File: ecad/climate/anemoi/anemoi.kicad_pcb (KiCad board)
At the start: 2 copper layers, 45 x 30 mm, 21 parts, among them J1 215079-4, SW1 219-3MST, U1 TMP1075DGK, U2 MMA8453Q, U3 HIH6131-021-001

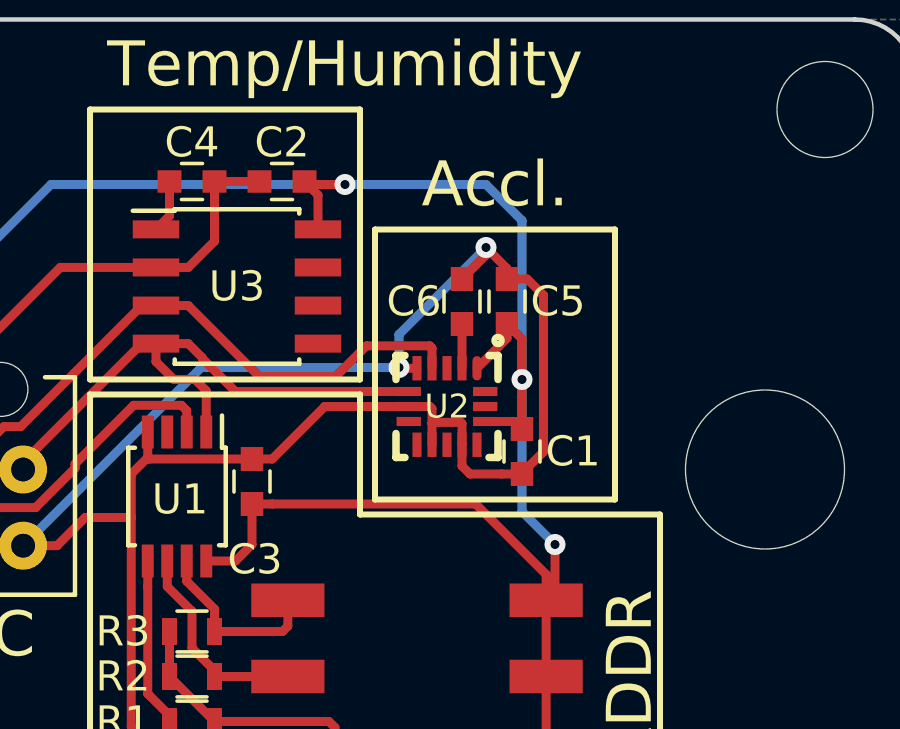
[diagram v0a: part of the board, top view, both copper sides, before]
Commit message: Updates Via size to conform to Factory Capabilities
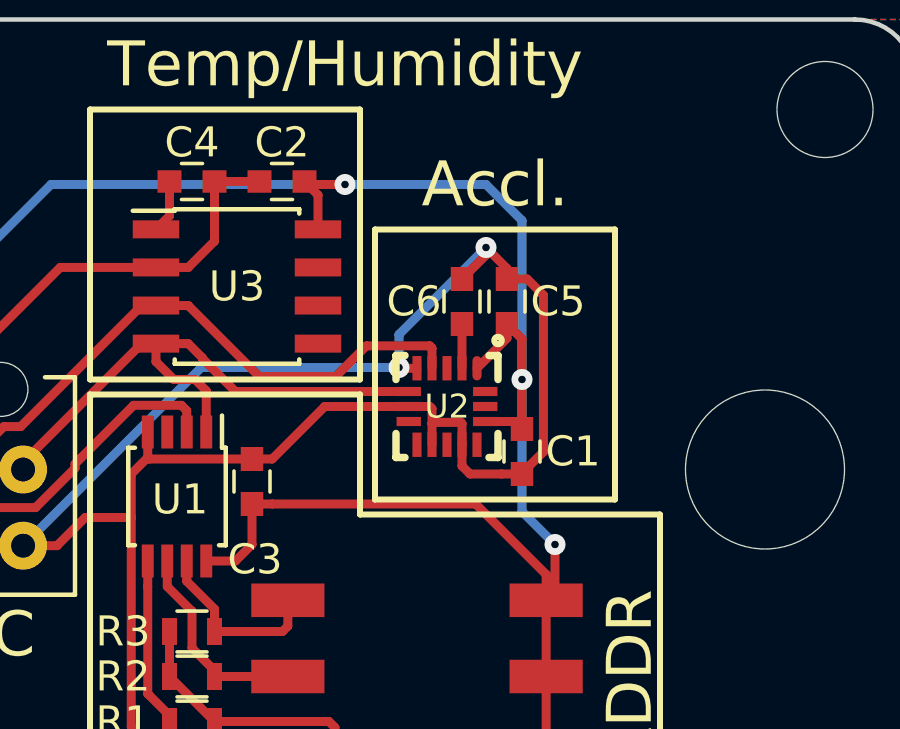
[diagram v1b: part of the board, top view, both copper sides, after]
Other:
- net class Default: via_drill 0.3 -> 0.25
- rule via_min_drill: 0.3 -> 0.25
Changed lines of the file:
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@@
-(kicad_pcb (version 4) (host pcbnew 4.0.7+dfsg1-1~bpo9+1)
+(kicad_pcb (version 20171130) (host pcbnew 5.0.0+dfsg1-2~bpo9+1)
   (general
-    (links 40)
-    (no_connects 0)
-    (area 69.924999 84.924999 115.075001 115.075001)
     (thickness 1.6)
     (drawings 30)
@@
     (edge_width 0.15)
     (via_size 0.7)
-    (via_drill 0.3)
+    (via_drill 0.25)
     (via_min_size 0.4)
-    (via_min_drill 0.3)
+    (via_min_drill 0.25)
     (uvia_size 0.3)
     (uvia_drill 0.1)
@@
       (layerselection 0x00030_80000001)
       (usegerberextensions false)
+      (usegerberattributes false)
+      (usegerberadvancedattributes false)
+      (creategerberjobfile false)
       (excludeedgelayer true)
       (linewidth 0.100000)
@@
       (hpglpennumber 1)
       (hpglpenspeed 20)
-      (hpglpendiameter 15)
-      (hpglpenoverlay 2)
+      (hpglpendiameter 15.000000)
       (psnegative false)
       (psa4output false)
@@
     (trace_width 0.3)
     (via_dia 0.7)
-    (via_drill 0.3)
+    (via_drill 0.25)
     (uvia_dia 0.3)
     (uvia_drill 0.1)
@@
     (tags "capacitor 0603")
     (attr smd)
-    (fp_text reference C1 (at 0 -1.7 360) (layer F.SilkS)
+    (fp_text reference C1 (at 0 -1.7) (layer F.SilkS)
       (effects (font (size 1 1) (thickness 0.15)))
     )
@@
     (tags "SSOP 0.65")
     (attr smd)
-    (fp_text reference U1 (at 0.1 -0.1 540) (layer F.SilkS)
+    (fp_text reference U1 (at 0.1 -0.1 180) (layer F.SilkS)
       (effects (font (size 1 1) (thickness 0.15)))
     )
@@
   (module FORT:Freescale_98ASA00063D_3x3mm_Pitch_0.5mm (layer F.Cu)
     (at 99.4 97.9 270)
-    (fp_text reference U2 (at 0 0 360) (layer F.SilkS)
+    (fp_text reference U2 (at 0 0) (layer F.SilkS)
       (effects (font (size 0.8 0.8) (thickness 0.15)))
     )
@@
   (segment (start 100.7 92.6) (end 100.7 92.85) (width 0.3) (layer F.Cu) (net 1))
   (segment (start 100.7 92.85) (end 99.9 93.65) (width 0.3) (layer F.Cu) (net 1))
-  (via (at 100.7 92.6) (size 0.7) (drill 0.3) (layers F.Cu B.Cu) (net 1))
+  (via (at 100.7 92.6) (size 0.7) (drill 0.25) (layers F.Cu B.Cu) (net 1))
   (segment (start 98.4 96.625) (end 97.825 96.625) (width 0.3) (layer F.Cu) (net 1))
-  (via (at 97.8 96.6) (size 0.7) (drill 0.3) (layers F.Cu B.Cu) (net 1))
+  (via (at 97.8 96.6) (size 0.7) (drill 0.25) (layers F.Cu B.Cu) (net 1))
   (segment (start 97.825 96.625) (end 97.8 96.6) (width 0.3) (layer F.Cu) (net 1))
   (segment (start 92.9 99.65) (end 89.475 99.65) (width 0.3) (layer F.Cu) (net 1))
@@
   (segment (start 101.9 97) (end 101.9 101.4) (width 0.3) (layer B.Cu) (net 2))
   (segment (start 101.9 101.4) (end 103 102.5) (width 0.3) (layer B.Cu) (net 2))
-  (via (at 103 102.5) (size 0.7) (drill 0.3) (layers F.Cu B.Cu) (net 2))
+  (via (at 103 102.5) (size 0.7) (drill 0.25) (layers F.Cu B.Cu) (net 2))
   (segment (start 100.7 90.5) (end 101.9 91.7) (width 0.3) (layer B.Cu) (net 2))
   (segment (start 101.9 91.7) (end 101.9 97) (width 0.3) (layer B.Cu) (net 2))
@@
   (segment (start 82.73 93.97) (end 86.2 90.5) (width 0.3) (layer B.Cu) (net 2))
   (segment (start 86.2 90.5) (end 96 90.5) (width 0.3) (layer B.Cu) (net 2))
-  (via (at 96 90.5) (size 0.7) (drill 0.3) (layers F.Cu B.Cu) (net 2))
+  (via (at 96 90.5) (size 0.7) (drill 0.25) (layers F.Cu B.Cu) (net 2))
   (segment (start 82.73 98.73) (end 82.73 93.97) (width 0.3) (layer B.Cu) (net 2))
   (segment (start 95.1 91.995) (end 95.1 90.85) (width 0.3) (layer F.Cu) (net 2))
@@
   (segment (start 101.4 95.625) (end 100.4 96.625) (width 0.3) (layer F.Cu) (net 2))
   (segment (start 101.9 98.65) (end 101.9 97) (width 0.3) (layer F.Cu) (net 2))
-  (via (at 101.9 97) (size 0.7) (drill 0.3) (layers F.Cu B.Cu) (net 2))
+  (via (at 101.9 97) (size 0.7) (drill 0.25) (layers F.Cu B.Cu) (net 2))
   (segment (start 100.675 98.4) (end 101.65 98.4) (width 0.3) (layer F.Cu) (net 2))
   (segment (start 101.65 98.4) (end 101.9 98.65) (width 0.3) (layer F.Cu) (net 2))

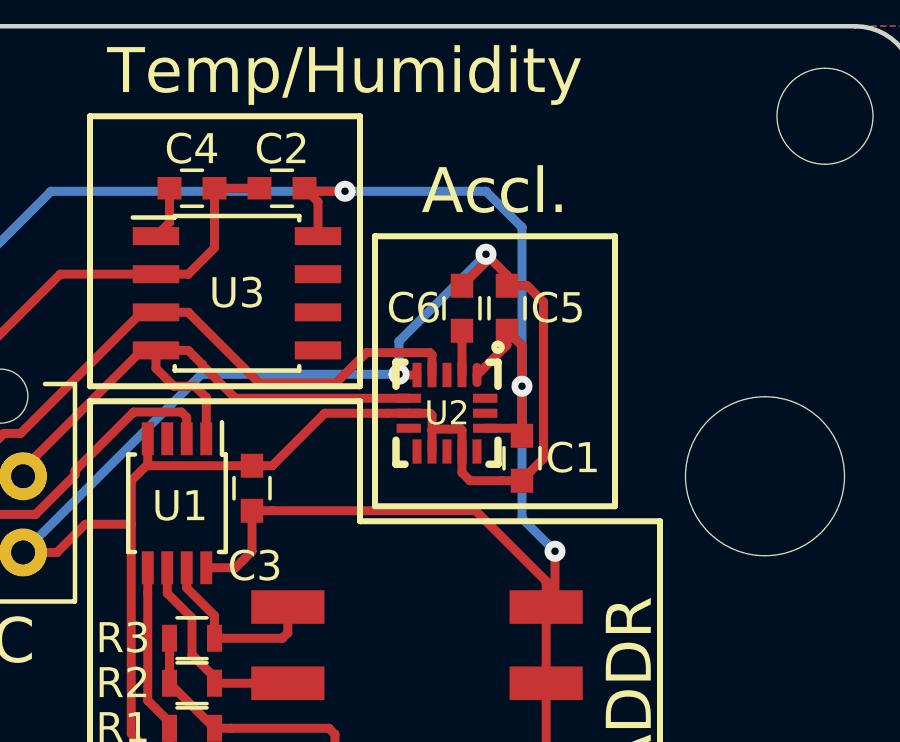
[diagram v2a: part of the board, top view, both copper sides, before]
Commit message: Changes via fpr ,ultiple factory capabilities
To be both eurocircuit and pcbway low price compatible, via should be
0.75/0.3 mm sized.
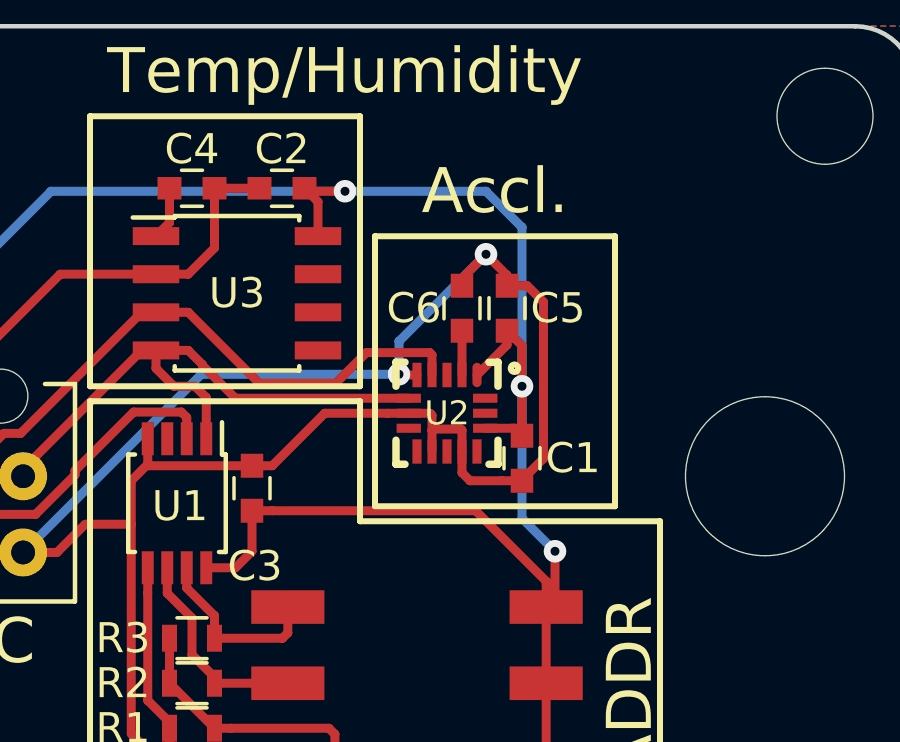
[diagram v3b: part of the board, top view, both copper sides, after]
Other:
- net class Default: via_dia 0.7 -> 0.75; via_drill 0.25 -> 0.3

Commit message: Licenses Climate PCB under OHL v1.2
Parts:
- added G***: LOGO, FORT:UNIL-LOGO_9.2x3, F.Cu at (112.5, 105.2)
- moved REF*** 33.9 mm to (110.5, 93.8), turned to 90 degrees
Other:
- board text added: "© 2018 UNIL"

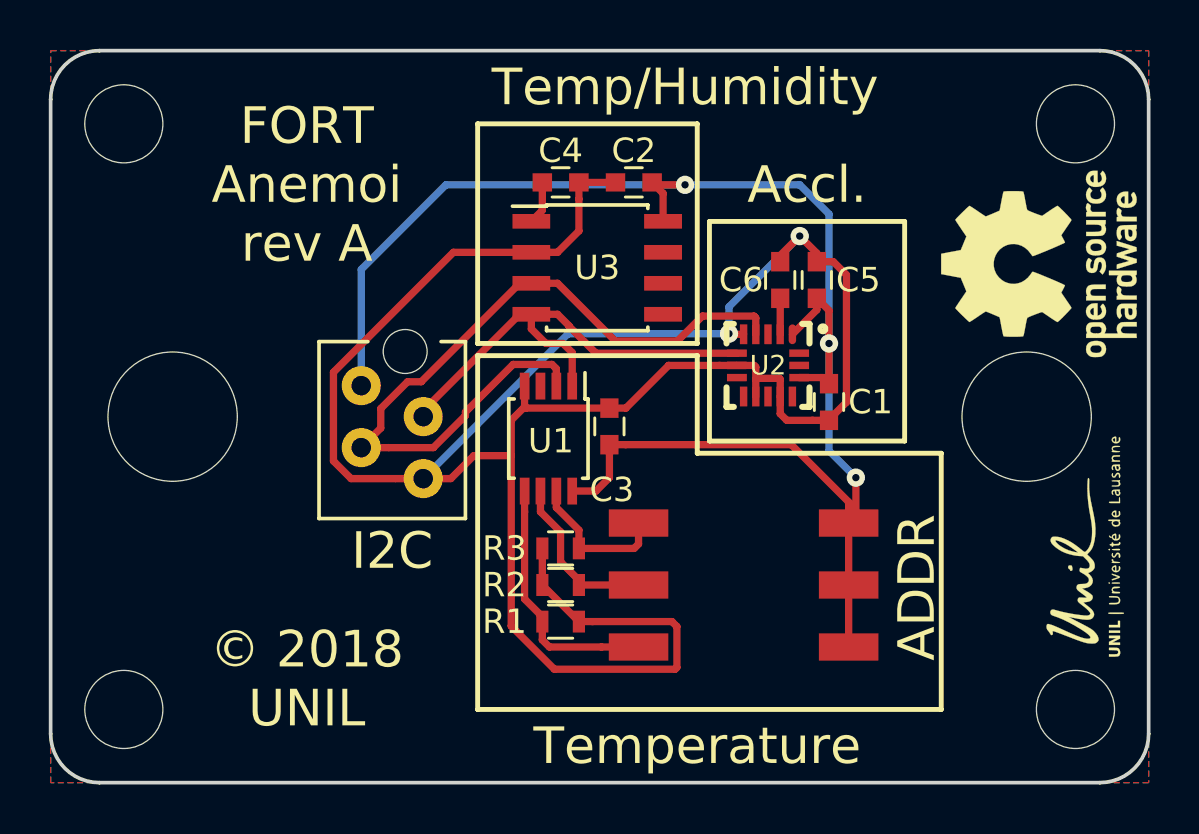
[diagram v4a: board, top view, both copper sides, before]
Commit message: Adds TVS on Anemoi
Super low capacitance TVS
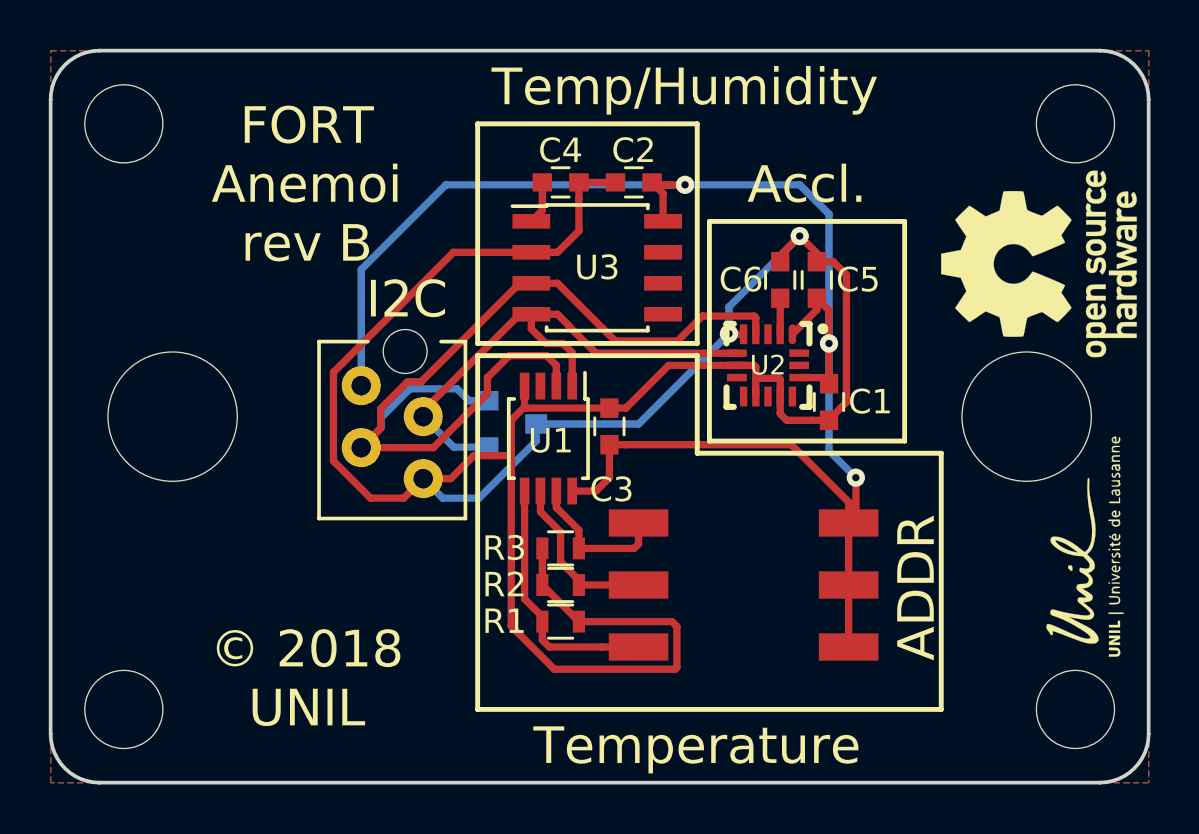
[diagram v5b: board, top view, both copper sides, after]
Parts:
- added D1: CPDT-5V0USP-HF, Package_TO_SOT_SMD:SOT-23, B.Cu at (88.9, 100.3)
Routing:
- net /SCL: track 31.8 -> 39.1 mm
- net /SDA: track 19.5 -> 22.6 mm
- net GND: track 101.8 -> 103.5 mm
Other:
- board text added: "FORT Anemoi rev B"
- board text removed: "FORT Anemoi rev A"

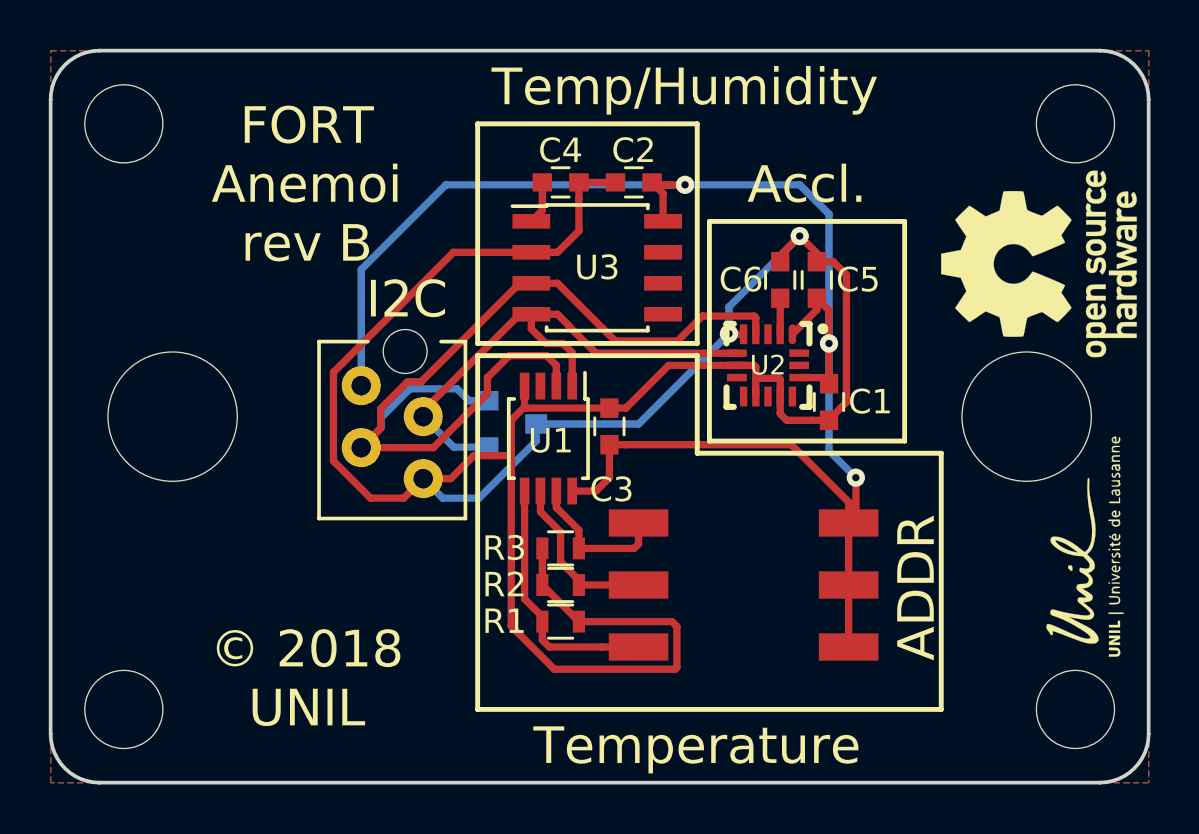
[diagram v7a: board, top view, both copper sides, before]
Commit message: Updates anemoi to KiCad v8
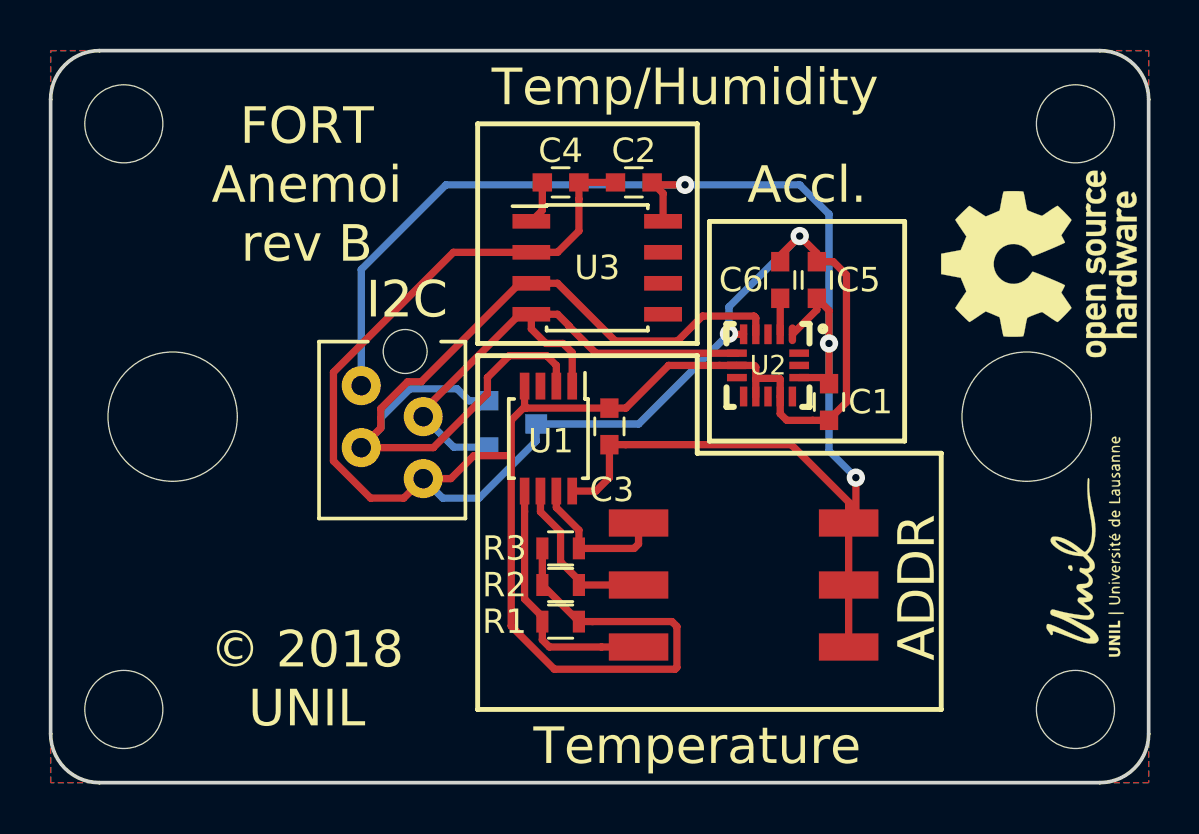
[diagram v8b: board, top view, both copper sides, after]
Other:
- net class Default removed
